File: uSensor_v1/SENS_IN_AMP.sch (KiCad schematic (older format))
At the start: 8 parts, among them U16 TBD

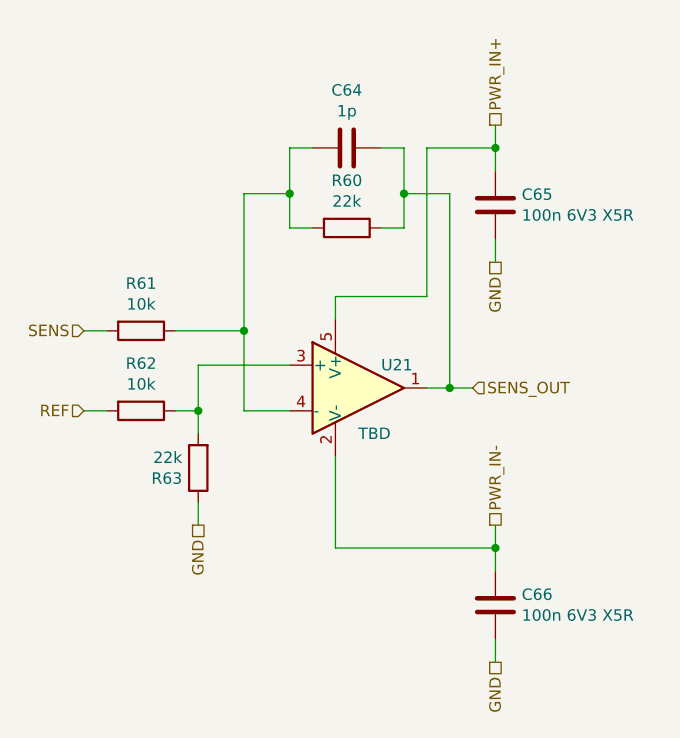
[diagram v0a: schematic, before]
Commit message: Added testpoints to schematic.
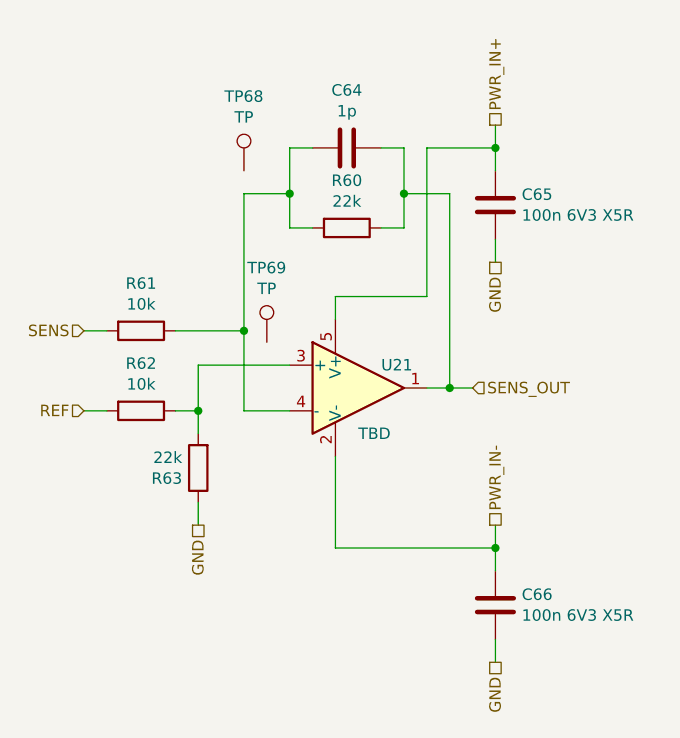
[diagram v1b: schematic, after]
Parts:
- added TP66, TP67: TP, Sentisa-Connectors:TestPoint_Probe_1.0mmDiameter_0.6mmDrill, symbol Connector:TestPoint
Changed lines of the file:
@@
 Text HLabel 6000 4150 1    50   UnSpc ~ 0
 PWR_IN-
+$Comp
+L Connector:TestPoint TP?
+U 1 1 5D2C6388
+P 4900 2600
+AR Path="/5D2C6388" Ref="TP?"  Part="1"
+AR Path="/5D0DF15B/5D2C6388" Ref="TP66"  Part="1"
+AR Path="/5C6EFF05/5D2C6388" Ref="TP62"  Part="1"
+AR Path="/5D09CD82/5D2C6388" Ref="TP64"  Part="1"
+AR Path="/5D1213F6/5D2C6388" Ref="TP68"  Part="1"
+F 0 "TP68" H 4900 2925 50  0000 C CNN
+F 1 "TP" H 4900 2834 50  0000 C CNN
+F 2 "Sentisa-Connectors:TestPoint_Probe_1.0mmDiameter_0.6mmDrill" H 5100 2600 50  0001 C CNN
+F 3 "~" H 5100 2600 50  0001 C CNN
+	1    4900 2600
+	1    0    0    -1
+$EndComp
+$Comp
+L Connector:TestPoint TP?
+U 1 1 5D2C69C6
+P 5000 3350
+AR Path="/5D2C69C6" Ref="TP?"  Part="1"
+AR Path="/5D0DF15B/5D2C69C6" Ref="TP67"  Part="1"
+AR Path="/5C6EFF05/5D2C69C6" Ref="TP63"  Part="1"
+AR Path="/5D09CD82/5D2C69C6" Ref="TP65"  Part="1"
+AR Path="/5D1213F6/5D2C69C6" Ref="TP69"  Part="1"
+F 0 "TP69" H 5000 3675 50  0000 C CNN
+F 1 "TP" H 5000 3584 50  0000 C CNN
+F 2 "Sentisa-Connectors:TestPoint_Probe_1.0mmDiameter_0.6mmDrill" H 5200 3350 50  0001 C CNN
+F 3 "~" H 5200 3350 50  0001 C CNN
+	1    5000 3350
+	1    0    0    -1
+$EndComp
 $EndSCHEMATC

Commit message: Schematic in progress.
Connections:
- net at R36.1, R37.2, U16.3 (+): now also TP67.1
- net at C51.2, R34.2, R35.1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: now also TP66.1
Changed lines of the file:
@@
 $Descr A4 11693 8268
 encoding utf-8
-Sheet 2 7
+Sheet 7 7
 Title ""
 Date ""
@@
 AR Path="/5D0DF15B/5C6F01FE" Ref="U20"  Part="1"
 AR Path="/5D1213F6/5C6F01FE" Ref="U21"  Part="1"
-F 0 "U21" H 5500 3650 50  0000 L CNN
+F 0 "U16" H 5500 3650 50  0000 L CNN
 F 1 "TBD" H 5400 3350 50  0000 L CNN
 F 2 "" H 5400 3550 50  0001 C CNN
@@
 AR Path="/5D0DF15B/5C6F0205" Ref="R58"  Part="1"
 AR Path="/5D1213F6/5C6F0205" Ref="R62"  Part="1"
-F 0 "R62" V 4243 3650 50  0000 C CNN
+F 0 "R36" V 4243 3650 50  0000 C CNN
 F 1 "10k" V 4334 3650 50  0000 C CNN
 F 2 "Resistor_SMD:R_0603_1608Metric_Pad1.05x0.95mm_HandSolder" V 4380 3650 50  0001 C CNN
@@
 AR Path="/5D0DF15B/5C6F020C" Ref="C61"  Part="1"
 AR Path="/5D1213F6/5C6F020C" Ref="C64"  Part="1"
-F 0 "C64" V 5098 2500 50  0000 C CNN
+F 0 "C51" V 5098 2500 50  0000 C CNN
 F 1 "1p" V 5189 2500 50  0000 C CNN
 F 2 "Capacitor_SMD:C_0603_1608Metric_Pad1.05x0.95mm_HandSolder" H 5388 2350 50  0001 C CNN
@@
 AR Path="/5D0DF15B/5C6F0213" Ref="R59"  Part="1"
 AR Path="/5D1213F6/5C6F0213" Ref="R63"  Part="1"
-F 0 "R63" H 4770 3946 50  0000 L CNN
+F 0 "R37" H 4770 3946 50  0000 L CNN
 F 1 "22k" H 4770 3855 50  0000 L CNN
 F 2 "Resistor_SMD:R_0603_1608Metric_Pad1.05x0.95mm_HandSolder" V 4630 3900 50  0001 C CNN
@@
 	4700 3650 4700 3450
 Wire Wire Line
-	4700 3450 5100 3450
+	4700 3450 5000 3450
 Connection ~ 4700 3650
 $Comp
@@
 AR Path="/5D0DF15B/5C6F0221" Ref="R57"  Part="1"
 AR Path="/5D1213F6/5C6F0221" Ref="R61"  Part="1"
-F 0 "R61" V 4243 3300 50  0000 C CNN
+F 0 "R35" V 4243 3300 50  0000 C CNN
 F 1 "10k" V 4334 3300 50  0000 C CNN
 F 2 "Resistor_SMD:R_0603_1608Metric_Pad1.05x0.95mm_HandSolder" V 4380 3300 50  0001 C CNN
@@
 AR Path="/5D0DF15B/5C6F0228" Ref="R56"  Part="1"
 AR Path="/5D1213F6/5C6F0228" Ref="R60"  Part="1"
-F 0 "R60" V 5143 2850 50  0000 C CNN
+F 0 "R34" V 5143 2850 50  0000 C CNN
 F 1 "22k" V 5234 2850 50  0000 C CNN
 F 2 "Resistor_SMD:R_0603_1608Metric_Pad1.05x0.95mm_HandSolder" V 5280 2850 50  0001 C CNN
@@
 AR Path="/5D0DF15B/5C6F0253" Ref="C62"  Part="1"
 AR Path="/5D1213F6/5C6F0253" Ref="C65"  Part="1"
-F 0 "C65" H 6115 2796 50  0000 L CNN
+F 0 "C52" H 6115 2796 50  0000 L CNN
 F 1 "100n 6V3 X5R" H 6115 2705 50  0000 L CNN
 F 2 "Capacitor_SMD:C_0603_1608Metric_Pad1.05x0.95mm_HandSolder" H 6038 2600 50  0001 C CNN
@@
 AR Path="/5D0DF15B/5C6F0260" Ref="C63"  Part="1"
 AR Path="/5D1213F6/5C6F0260" Ref="C66"  Part="1"
-F 0 "C66" H 6115 4546 50  0000 L CNN
+F 0 "C53" H 6115 4546 50  0000 L CNN
 F 1 "100n 6V3 X5R" H 6115 4455 50  0000 L CNN
 F 2 "Capacitor_SMD:C_0603_1608Metric_Pad1.05x0.95mm_HandSolder" H 6038 4350 50  0001 C CNN
@@
 AR Path="/5D09CD82/5D2C6388" Ref="TP64"  Part="1"
 AR Path="/5D1213F6/5D2C6388" Ref="TP68"  Part="1"
-F 0 "TP68" H 4900 2925 50  0000 C CNN
+F 0 "TP62" H 4900 2925 50  0000 C CNN
 F 1 "TP" H 4900 2834 50  0000 C CNN
 F 2 "Sentisa-Connectors:TestPoint_Probe_1.0mmDiameter_0.6mmDrill" H 5100 2600 50  0001 C CNN
@@
 AR Path="/5D09CD82/5D2C69C6" Ref="TP65"  Part="1"
 AR Path="/5D1213F6/5D2C69C6" Ref="TP69"  Part="1"
-F 0 "TP69" H 5000 3675 50  0000 C CNN
+F 0 "TP63" H 5000 3675 50  0000 C CNN
 F 1 "TP" H 5000 3584 50  0000 C CNN
 F 2 "Sentisa-Connectors:TestPoint_Probe_1.0mmDiameter_0.6mmDrill" H 5200 3350 50  0001 C CNN
@@
 	1    0    0    -1
 $EndComp
+Wire Wire Line
+	5000 3350 5000 3450
+Connection ~ 5000 3450
+Wire Wire Line
+	5000 3450 5100 3450
+Wire Wire Line
+	4900 2600 4900 2700
+Connection ~ 4900 2700
 $EndSCHEMATC

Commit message: Schematic checked.
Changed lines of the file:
@@
 AR Path="/5D0DF15B/5C6F01FE" Ref="U20"  Part="1"
 AR Path="/5D1213F6/5C6F01FE" Ref="U21"  Part="1"
-F 0 "U16" H 5500 3650 50  0000 L CNN
+F 0 "U21" H 5500 3650 50  0000 L CNN
 F 1 "TBD" H 5400 3350 50  0000 L CNN
 F 2 "" H 5400 3550 50  0001 C CNN
@@
 AR Path="/5D0DF15B/5C6F0205" Ref="R58"  Part="1"
 AR Path="/5D1213F6/5C6F0205" Ref="R62"  Part="1"
-F 0 "R36" V 4243 3650 50  0000 C CNN
+F 0 "R62" V 4243 3650 50  0000 C CNN
 F 1 "10k" V 4334 3650 50  0000 C CNN
 F 2 "Resistor_SMD:R_0603_1608Metric_Pad1.05x0.95mm_HandSolder" V 4380 3650 50  0001 C CNN
@@
 AR Path="/5D0DF15B/5C6F020C" Ref="C61"  Part="1"
 AR Path="/5D1213F6/5C6F020C" Ref="C64"  Part="1"
-F 0 "C51" V 5098 2500 50  0000 C CNN
+F 0 "C64" V 5098 2500 50  0000 C CNN
 F 1 "1p" V 5189 2500 50  0000 C CNN
 F 2 "Capacitor_SMD:C_0603_1608Metric_Pad1.05x0.95mm_HandSolder" H 5388 2350 50  0001 C CNN
@@
 AR Path="/5D0DF15B/5C6F0213" Ref="R59"  Part="1"
 AR Path="/5D1213F6/5C6F0213" Ref="R63"  Part="1"
-F 0 "R37" H 4770 3946 50  0000 L CNN
+F 0 "R63" H 4770 3946 50  0000 L CNN
 F 1 "22k" H 4770 3855 50  0000 L CNN
 F 2 "Resistor_SMD:R_0603_1608Metric_Pad1.05x0.95mm_HandSolder" V 4630 3900 50  0001 C CNN
@@
 AR Path="/5D0DF15B/5C6F0221" Ref="R57"  Part="1"
 AR Path="/5D1213F6/5C6F0221" Ref="R61"  Part="1"
-F 0 "R35" V 4243 3300 50  0000 C CNN
+F 0 "R61" V 4243 3300 50  0000 C CNN
 F 1 "10k" V 4334 3300 50  0000 C CNN
 F 2 "Resistor_SMD:R_0603_1608Metric_Pad1.05x0.95mm_HandSolder" V 4380 3300 50  0001 C CNN
@@
 AR Path="/5D0DF15B/5C6F0228" Ref="R56"  Part="1"
 AR Path="/5D1213F6/5C6F0228" Ref="R60"  Part="1"
-F 0 "R34" V 5143 2850 50  0000 C CNN
+F 0 "R60" V 5143 2850 50  0000 C CNN
 F 1 "22k" V 5234 2850 50  0000 C CNN
 F 2 "Resistor_SMD:R_0603_1608Metric_Pad1.05x0.95mm_HandSolder" V 5280 2850 50  0001 C CNN
@@
 AR Path="/5D0DF15B/5C6F0253" Ref="C62"  Part="1"
 AR Path="/5D1213F6/5C6F0253" Ref="C65"  Part="1"
-F 0 "C52" H 6115 2796 50  0000 L CNN
+F 0 "C65" H 6115 2796 50  0000 L CNN
 F 1 "100n 6V3 X5R" H 6115 2705 50  0000 L CNN
 F 2 "Capacitor_SMD:C_0603_1608Metric_Pad1.05x0.95mm_HandSolder" H 6038 2600 50  0001 C CNN
@@
 AR Path="/5D0DF15B/5C6F0260" Ref="C63"  Part="1"
 AR Path="/5D1213F6/5C6F0260" Ref="C66"  Part="1"
-F 0 "C53" H 6115 4546 50  0000 L CNN
+F 0 "C66" H 6115 4546 50  0000 L CNN
 F 1 "100n 6V3 X5R" H 6115 4455 50  0000 L CNN
 F 2 "Capacitor_SMD:C_0603_1608Metric_Pad1.05x0.95mm_HandSolder" H 6038 4350 50  0001 C CNN
@@
 AR Path="/5D09CD82/5D2C6388" Ref="TP64"  Part="1"
 AR Path="/5D1213F6/5D2C6388" Ref="TP68"  Part="1"
-F 0 "TP62" H 4900 2925 50  0000 C CNN
+F 0 "TP68" H 4900 2925 50  0000 C CNN
 F 1 "TP" H 4900 2834 50  0000 C CNN
 F 2 "Sentisa-Connectors:TestPoint_Probe_1.0mmDiameter_0.6mmDrill" H 5100 2600 50  0001 C CNN
@@
 AR Path="/5D09CD82/5D2C69C6" Ref="TP65"  Part="1"
 AR Path="/5D1213F6/5D2C69C6" Ref="TP69"  Part="1"
-F 0 "TP63" H 5000 3675 50  0000 C CNN
+F 0 "TP69" H 5000 3675 50  0000 C CNN
 F 1 "TP" H 5000 3584 50  0000 C CNN
 F 2 "Sentisa-Connectors:TestPoint_Probe_1.0mmDiameter_0.6mmDrill" H 5200 3350 50  0001 C CNN

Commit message: Schematic in progress.
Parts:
- C51: value 1p -> 1p 16V X5R
- R34, R37: value 22k -> 22k 1%
- R35, R36: value 10k -> 10k 1%
- U16: footprint (none) -> TBD; symbol Amplifier_Operational:AD8603 -> Amplifier_Operational:LM321; MFR (none) -> TBD; MPN (none) -> TBD
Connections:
- net SENS_OUT: now also U16.4; no longer U16.1
- net at R36.1, R37.2, TP67.1: now also U16.1 (+); no longer U16.3 (+)
- net at C51.2, R34.2, R35.1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: now also U16.3 (-); no longer U16.4 (-)
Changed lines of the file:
@@
 $Descr A4 11693 8268
 encoding utf-8
-Sheet 7 7
+Sheet 2 7
 Title ""
 Date ""
@@
 $EndDescr
 $Comp
-L Amplifier_Operational:AD8603 U?
+L Amplifier_Operational:LM321 U?
 U 1 1 5C6F01FE
 P 5400 3550
@@
 AR Path="/5D0DF15B/5C6F01FE" Ref="U20"  Part="1"
 AR Path="/5D1213F6/5C6F01FE" Ref="U21"  Part="1"
-F 0 "U21" H 5500 3650 50  0000 L CNN
+F 0 "U16" H 5500 3650 50  0000 L CNN
 F 1 "TBD" H 5400 3350 50  0000 L CNN
-F 2 "" H 5400 3550 50  0001 C CNN
-F 3 "http://www.analog.com/media/en/technical-documentation/data-sheets/AD8603_8607_8609.pdf" H 5400 3750 50  0001 C CNN
+F 2 "TBD" H 5400 3550 50  0001 C CNN
+F 3 "" H 5400 3750 50  0001 C CNN
+F 4 "TBD" H 5400 3550 50  0001 C CNN "MFR"
+F 5 "TBD" H 5400 3550 50  0001 C CNN "MPN"
 	1    5400 3550
 	1    0    0    -1
@@
 AR Path="/5D0DF15B/5C6F0205" Ref="R58"  Part="1"
 AR Path="/5D1213F6/5C6F0205" Ref="R62"  Part="1"
-F 0 "R62" V 4243 3650 50  0000 C CNN
-F 1 "10k" V 4334 3650 50  0000 C CNN
+F 0 "R36" V 4243 3650 50  0000 C CNN
+F 1 "10k 1%" V 4334 3650 50  0000 C CNN
 F 2 "Resistor_SMD:R_0603_1608Metric_Pad1.05x0.95mm_HandSolder" V 4380 3650 50  0001 C CNN
 F 3 "~" H 4450 3650 50  0001 C CNN
@@
 AR Path="/5D0DF15B/5C6F020C" Ref="C61"  Part="1"
 AR Path="/5D1213F6/5C6F020C" Ref="C64"  Part="1"
-F 0 "C64" V 5098 2500 50  0000 C CNN
-F 1 "1p" V 5189 2500 50  0000 C CNN
+F 0 "C51" V 5098 2500 50  0000 C CNN
+F 1 "1p 16V X5R" V 5189 2500 50  0000 C CNN
 F 2 "Capacitor_SMD:C_0603_1608Metric_Pad1.05x0.95mm_HandSolder" H 5388 2350 50  0001 C CNN
 F 3 "~" H 5350 2500 50  0001 C CNN
@@
 AR Path="/5D0DF15B/5C6F0213" Ref="R59"  Part="1"
 AR Path="/5D1213F6/5C6F0213" Ref="R63"  Part="1"
-F 0 "R63" H 4770 3946 50  0000 L CNN
-F 1 "22k" H 4770 3855 50  0000 L CNN
+F 0 "R37" H 4630 3854 50  0000 R CNN
+F 1 "22k 1%" H 4630 3945 50  0000 R CNN
 F 2 "Resistor_SMD:R_0603_1608Metric_Pad1.05x0.95mm_HandSolder" V 4630 3900 50  0001 C CNN
 F 3 "~" H 4700 3900 50  0001 C CNN
@@
 AR Path="/5D0DF15B/5C6F0221" Ref="R57"  Part="1"
 AR Path="/5D1213F6/5C6F0221" Ref="R61"  Part="1"
-F 0 "R61" V 4243 3300 50  0000 C CNN
-F 1 "10k" V 4334 3300 50  0000 C CNN
+F 0 "R35" V 4243 3300 50  0000 C CNN
+F 1 "10k 1%" V 4334 3300 50  0000 C CNN
 F 2 "Resistor_SMD:R_0603_1608Metric_Pad1.05x0.95mm_HandSolder" V 4380 3300 50  0001 C CNN
 F 3 "~" H 4450 3300 50  0001 C CNN
@@
 AR Path="/5D0DF15B/5C6F0228" Ref="R56"  Part="1"
 AR Path="/5D1213F6/5C6F0228" Ref="R60"  Part="1"
-F 0 "R60" V 5143 2850 50  0000 C CNN
-F 1 "22k" V 5234 2850 50  0000 C CNN
+F 0 "R34" V 5143 2850 50  0000 C CNN
+F 1 "22k 1%" V 5234 2850 50  0000 C CNN
 F 2 "Resistor_SMD:R_0603_1608Metric_Pad1.05x0.95mm_HandSolder" V 5280 2850 50  0001 C CNN
 F 3 "~" H 5350 2850 50  0001 C CNN
@@
 AR Path="/5D0DF15B/5C6F0253" Ref="C62"  Part="1"
 AR Path="/5D1213F6/5C6F0253" Ref="C65"  Part="1"
-F 0 "C65" H 6115 2796 50  0000 L CNN
+F 0 "C52" H 6115 2796 50  0000 L CNN
 F 1 "100n 6V3 X5R" H 6115 2705 50  0000 L CNN
 F 2 "Capacitor_SMD:C_0603_1608Metric_Pad1.05x0.95mm_HandSolder" H 6038 2600 50  0001 C CNN
@@
 AR Path="/5D0DF15B/5C6F0260" Ref="C63"  Part="1"
 AR Path="/5D1213F6/5C6F0260" Ref="C66"  Part="1"
-F 0 "C66" H 6115 4546 50  0000 L CNN
+F 0 "C53" H 6115 4546 50  0000 L CNN
 F 1 "100n 6V3 X5R" H 6115 4455 50  0000 L CNN
 F 2 "Capacitor_SMD:C_0603_1608Metric_Pad1.05x0.95mm_HandSolder" H 6038 4350 50  0001 C CNN
@@
 AR Path="/5D09CD82/5D2C6388" Ref="TP64"  Part="1"
 AR Path="/5D1213F6/5D2C6388" Ref="TP68"  Part="1"
-F 0 "TP68" H 4900 2925 50  0000 C CNN
+F 0 "TP62" H 4900 2925 50  0000 C CNN
 F 1 "TP" H 4900 2834 50  0000 C CNN
 F 2 "Sentisa-Connectors:TestPoint_Probe_1.0mmDiameter_0.6mmDrill" H 5100 2600 50  0001 C CNN
@@
 AR Path="/5D09CD82/5D2C69C6" Ref="TP65"  Part="1"
 AR Path="/5D1213F6/5D2C69C6" Ref="TP69"  Part="1"
-F 0 "TP69" H 5000 3675 50  0000 C CNN
+F 0 "TP63" H 5000 3675 50  0000 C CNN
 F 1 "TP" H 5000 3584 50  0000 C CNN
 F 2 "Sentisa-Connectors:TestPoint_Probe_1.0mmDiameter_0.6mmDrill" H 5200 3350 50  0001 C CNN
